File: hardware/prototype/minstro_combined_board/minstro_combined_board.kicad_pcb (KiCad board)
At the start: 4 copper layers, 130 x 100 mm, 130 parts, among them J1001 VFO, J301 BATT, J401 BOOT, J402 UART, J403 USB_C_Receptacle_USB2.0_16P, J404 SDMMC 4b, J405 Conn_Coaxial, J501 Headset, J601 FT6236_Conn_01x06, J602 ILI9488_Conn, J603 ST7789_Conn_01x12, J701 SOICbite-SWD, J801 NAV CONN, Q601 2N7002, SW401 RST, SW801 Navigation_Encoder_Joystick_S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, U201 LMR36006, U301 BQ24074RGT, U401 ESP32-S3, U402 W25Q128JVS, U701 ATSAMD10D13A-M, Y401 40 MHz

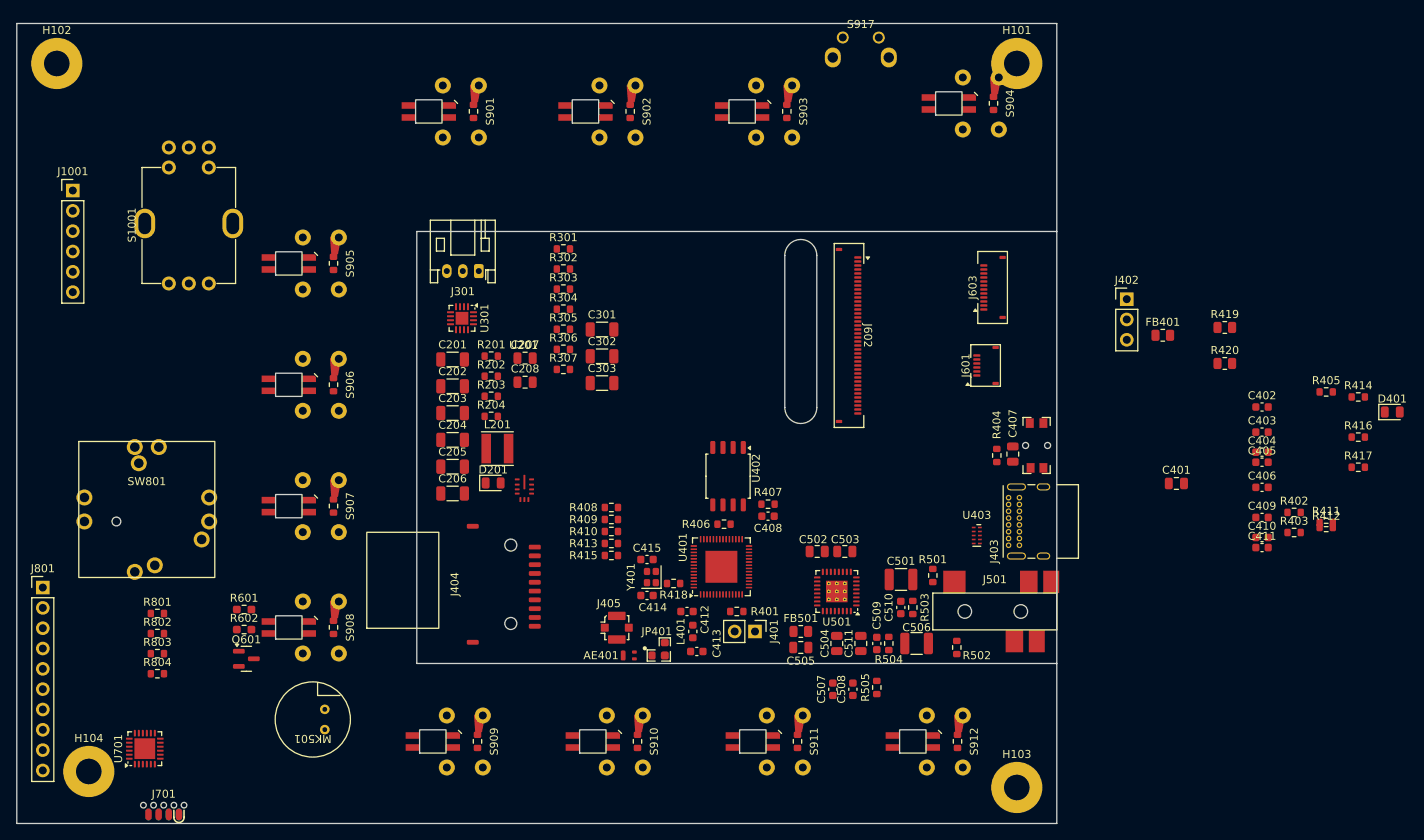
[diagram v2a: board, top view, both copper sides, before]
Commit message: Layout and routing Power and initial signals, SD card
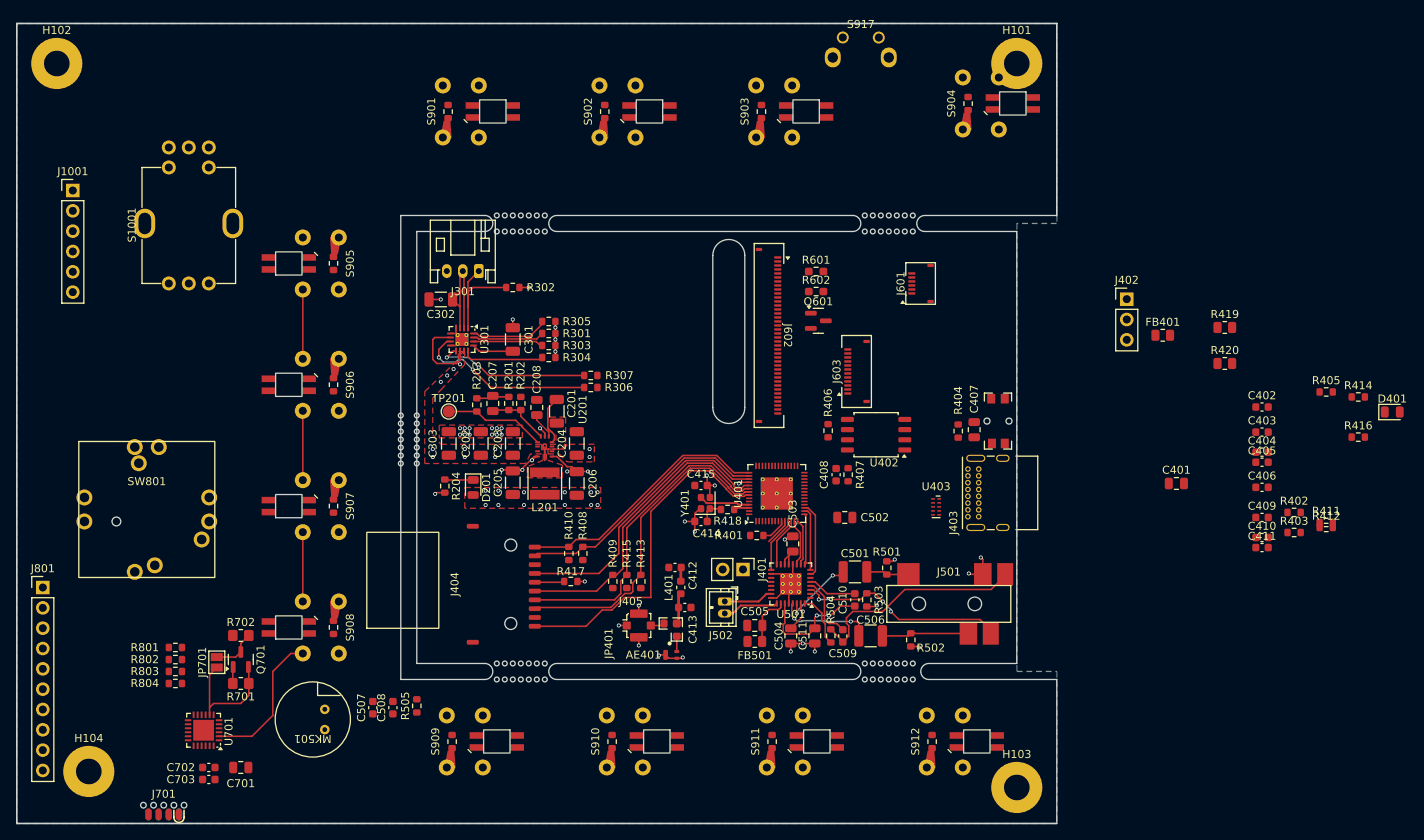
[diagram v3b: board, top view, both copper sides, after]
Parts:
- added C701: 10uF, Capacitor_SMD:C_0805_2012Metric, F.Cu at (93.0, 133.0)
- added C702: 0.1uF, Capacitor_SMD:C_0603_1608Metric, F.Cu at (89.0, 133.0)
- added C703: 0.1uF, Capacitor_SMD:C_0603_1608Metric, F.Cu at (89.0, 134.5)
- added J502: SPKR, Connector_JST:JST_ZH_B2B-ZR_1x02_P1.50mm_Vertical, F.Cu at (153.5, 112.2)
- added JP701: Jumper_2_Open, Jumper:SolderJumper-2_P1.3mm_Open_Pad1.0x1.5mm, F.Cu at (90.0, 119.8)
- added Q701: 2N7002, Package_TO_SOT_SMD:SOT-23, F.Cu at (93.0, 119.5)
- added R701: 10k, Resistor_SMD:R_0805_2012Metric_Pad1.20x1.40mm_HandSolder, F.Cu at (93.0, 122.5)
- added R702: 10k, Resistor_SMD:R_0805_2012Metric_Pad1.20x1.40mm_HandSolder, F.Cu at (93.0, 116.5)
- added REF**: Untitled, BVH_Features:MouseBite_2mm_7holes, F.Cu at (174.0, 65.0)
- added REF**: Untitled, BVH_Features:MouseBite_2mm_7holes, F.Cu at (174.0, 121.0)
- added REF**: Untitled, BVH_Features:MouseBite_2mm_7holes, F.Cu at (128.0, 65.0)
- added REF**: Untitled, BVH_Features:MouseBite_2mm_7holes, F.Cu at (128.0, 121.0)
- added REF**: Untitled, BVH_Features:MouseBite_2mm_7holes, F.Cu at (114.0, 92.0)
- added TP201: TestPoint, TestPoint:TestPoint_Pad_D1.5mm, F.Cu at (119.0, 88.5)
- U301: footprint Package_DFN_QFN:VQFN-16-1EP_3x3mm_P0.5mm_EP1.6x1.6mm -> Package_DFN_QFN:VQFN-16-1EP_3x3mm_P0.5mm_EP1.6x1.6mm_ThermalVias
- U401: footprint Package_DFN_QFN:QFN-56-1EP_7x7mm_P0.4mm_EP4x4mm -> Package_DFN_QFN:QFN-56-1EP_7x7mm_P0.4mm_EP4x4mm_ThermalVias
- moved R417 99.5 mm to (134.2, 109.8), turned to 180 degrees
- moved Q601 83.1 mm to (165.2, 77.2)
- moved R601 83.1 mm to (164.9, 71.0)
- moved R602 83.1 mm to (164.9, 73.5)
- moved C507 57.5 mm to (109.5, 125.5)
- moved R505 57.5 mm to (115.0, 125.3)
- moved C508 57.5 mm to (112.0, 125.5)
- moved C302 21.4 mm to (118.0, 74.5), turned to 180 degrees
- moved C303 20.6 mm to (119.0, 92.5), turned to 90 degrees
- moved J603 20.0 mm to (170.0, 83.5)
- moved U402 19.2 mm to (172.4, 91.4), turned to 180 degrees
- moved R406 17.5 mm to (166.4, 90.9), turned to -90 degrees
- moved C206 15.6 mm to (135.0, 97.5), turned to 90 degrees
- moved C204 15.5 mm to (135.0, 92.5), turned to 90 degrees
- moved C201 14.5 mm to (132.5, 88.5), turned to -90 degrees
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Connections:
- C511 pad 2: GNDA -> GND
- J301 pad 1: GND -> /Battery/BATT_TS
- J301 pad 3: /Battery/BATT_TS -> GND
- U401 pad 13: /Display Connectors/DISP_DC -> /Audio/I2S_MCLK
- U401 pad 14: /Display Connectors/DISP_CS -> /Audio/I2S_ADCIN
- U401 pad 15: /Display Connectors/DISP_SCL -> /Audio/I2S_ADCOUT
- U401 pad 16: /Display Connectors/DISP_SDA -> /Audio/I2S_BCLK
- U401 pad 17: /Display Connectors/DISP_RST -> /Audio/I2S_FS
- U401 pad 18: /Display Connectors/DISP_TS_INT -> /Display Connectors/DISP_DC
- U401 pad 19: /Display Connectors/DISP_TS_RST -> /Display Connectors/DISP_SCL
- U401 pad 21: /Battery/PWR_CHRG -> /Display Connectors/DISP_TS_INT
- U401 pad 22: /Battery/PWR_GOOD -> /Display Connectors/DISP_TS_RST
- U401 pad 23: unconnected-(U401-GPIO17-Pad23) -> /Display Connectors/DISP_SDA
- U401 pad 24: /ESP32 Microcontroller/SD_DET -> /Display Connectors/DISP_RST
- U401 pad 27: /Display Connectors/DISP_BL -> /Display Connectors/DISP_CS
- U401 pad 38: /Audio/I2S_FS -> /Display Connectors/DISP_BL
- U401 pad 39: /Audio/I2S_BCLK -> unconnected-(U401-GPIO34-Pad39)
- U401 pad 40: /Audio/I2S_ADCOUT -> unconnected-(U401-GPIO35-Pad40)
- U401 pad 41: /Audio/I2S_ADCIN -> /Battery/PWR_CHRG
- U401 pad 42: /Audio/I2S_MCLK -> /Battery/PWR_GOOD
- U401 pad 43: /ESP32 Microcontroller/SD_SCK -> /ESP32 Microcontroller/SD_DAT1
- U401 pad 45: /ESP32 Microcontroller/SD_DAT1 -> /ESP32 Microcontroller/SD_SCK
- U401 pad 47: /ESP32 Microcontroller/SD_DAT2 -> /ESP32 Microcontroller/SD_CMD
- U401 pad 49: /ESP32 Microcontroller/UART_TX -> /ESP32 Microcontroller/SD_DAT2
- U401 pad 50: /ESP32 Microcontroller/UART_RX -> /ESP32 Microcontroller/SD_DET
- U401 pad 51: /ESP32 Microcontroller/SD_CMD -> unconnected-(U401-GPIO45-Pad51)
- U401 pad 52: /ESP32 Microcontroller/SD_DET -> unconnected-(U401-GPIO46-Pad52)
- U501 pad 24: GNDA -> GND
- U501 pad 33: (no net) -> GND
- U701 pad 1: /HMI Controller/ROW_A -> /HMI Controller/ROW_C
- U701 pad 3: /HMI Controller/ROW_C -> unconnected-(U701-PA04-Pad3)
- U701 pad 4: /HMI Controller/ROW_D -> /HMI Controller/ROW_A
- U701 pad 8: /HMI Controller/RGB_DATA -> /HMI Controller/RGB_DATA_3.3
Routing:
- net GND: track 0.00 -> 59.3 mm, vias 0 -> 42
- net /HMI Controller/ROW_B: track 0.00 -> 44.0 mm
- net /ESP32 Microcontroller/SD_DET: track 0.00 -> 42.6 mm
- net /ESP32 Microcontroller/SD_DAT2: track 0.00 -> 40.4 mm
- net /ESP32 Microcontroller/SD_DAT3: track 0.00 -> 39.6 mm
- net /ESP32 Microcontroller/SD_CMD: track 0.00 -> 38.0 mm
- net /ESP32 Microcontroller/SD_SCK: track 0.00 -> 35.5 mm
- net /ESP32 Microcontroller/SD_DAT0: track 0.00 -> 32.8 mm
- net /ESP32 Microcontroller/SD_DAT1: track 0.00 -> 32.4 mm
- net /Audio/Mic_HS: track 0.00 -> 27.9 mm
- net /Audio/R_HS_N: track 0.00 -> 26.2 mm, vias 0 -> 4
- net /Battery/PWR_GOOD: track 0.00 -> 22.9 mm, vias 0 -> 2
- net /Battery/PWR_CHRG: track 0.00 -> 19.6 mm, vias 0 -> 2
- net +3.3V: track 0.00 -> 17.5 mm, vias 0 -> 16
- net +BATT: track 0.00 -> 17.1 mm
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- added copper zone on F.Cu, net +3.3V
- added copper zone on In2.Cu, net +3.3V
- added copper zone on F.Cu, net /Power/SW
- added copper zone on B.Cu, net GND
- added copper zone on F.Cu, net GND
- added copper zone on In1.Cu, net GND
- added copper zone on F.Cu, net Vdrive
- added copper zone on In2.Cu, net Vdrive
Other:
- outline, holes or cut-outs redrawn

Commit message: Layout WIP
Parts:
- moved C402 25.8 mm to (212.7, 112.5)
- moved C403 25.8 mm to (212.7, 115.6)
- moved C404 25.8 mm to (212.7, 118.1)
- moved C405 25.8 mm to (212.7, 119.4)
- moved C406 25.8 mm to (212.7, 122.5)
- moved R414 4.32 mm to (237.0, 86.5)
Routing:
- net /ESP32 Microcontroller/CHIP_EN: track 0.00 -> 11.7 mm
- net GND: track 59.3 -> 63.6 mm, vias 42 -> 45
- net +3.3V: track 17.5 -> 18.7 mm, vias 16 -> 17
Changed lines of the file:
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@@
 	(footprint "Capacitor_SMD:C_0603_1608Metric"
 		(layer "F.Cu")
-		(at 220.655 97.98)
+		(at 212.725 122.5)
 		(descr "Capacitor SMD 0603 (1608 Metric), square (rectangular) end terminal, IPC-7351 nominal, (Body size source: IPC-SM-782 page 76, https://www.pcb-3d.com/wordpress/wp-content/uploads/ipc-sm-782a_amendment_1_and_2.pdf), generated with kicad-footprint-generator")
 		(tags "capacitor")
@@
 	(footprint "Capacitor_SMD:C_0603_1608Metric"
 		(layer "F.Cu")
-		(at 220.655 87.94)
+		(at 212.725 112.46)
 		(descr "Capacitor SMD 0603 (1608 Metric), square (rectangular) end terminal, IPC-7351 nominal, (Body size source: IPC-SM-782 page 76, https://www.pcb-3d.com/wordpress/wp-content/uploads/ipc-sm-782a_amendment_1_and_2.pdf), generated with kicad-footprint-generator")
 		(tags "capacitor")
@@
 	(footprint "Capacitor_SMD:C_0603_1608Metric"
 		(layer "F.Cu")
-		(at 220.655 93.5875)
+		(at 212.725 118.1075)
 		(descr "Capacitor SMD 0603 (1608 Metric), square (rectangular) end terminal, IPC-7351 nominal, (Body size source: IPC-SM-782 page 76, https://www.pcb-3d.com/wordpress/wp-content/uploads/ipc-sm-782a_amendment_1_and_2.pdf), generated with kicad-footprint-generator")
 		(tags "capacitor")
@@
 		(tags "LED")
 		(property "Reference" "D401"
-			(at 0 -1.65 0)
+			(at -3.435 -0.0675 0)
 			(layer "F.SilkS")
 			(effects
@@
 	(footprint "Capacitor_SMD:C_0603_1608Metric"
 		(layer "F.Cu")
-		(at 220.655 94.8425)
+		(at 212.725 119.3625)
 		(descr "Capacitor SMD 0603 (1608 Metric), square (rectangular) end terminal, IPC-7351 nominal, (Body size source: IPC-SM-782 page 76, https://www.pcb-3d.com/wordpress/wp-content/uploads/ipc-sm-782a_amendment_1_and_2.pdf), generated with kicad-footprint-generator")
 		(tags "capacitor")
@@
 	(footprint "Resistor_SMD:R_0603_1608Metric"
 		(layer "F.Cu")
-		(at 232.685 86.685)
+		(at 237 86.5)
 		(descr "Resistor SMD 0603 (1608 Metric), square (rectangular) end terminal, IPC-7351 nominal, (Body size source: IPC-SM-782 page 72, https://www.pcb-3d.com/wordpress/wp-content/uploads/ipc-sm-782a_amendment_1_and_2.pdf), generated with kicad-footprint-generator")
 		(tags "resistor")
 		(property "Reference" "R414"
-			(at 0 -1.43 0)
+			(at -3.5 0 0)
 			(layer "F.SilkS")
 			(effects
@@
 	(footprint "Capacitor_SMD:C_0603_1608Metric"
 		(layer "F.Cu")
-		(at 220.655 91.0775)
+		(at 212.725 115.5975)
 		(descr "Capacitor SMD 0603 (1608 Metric), square (rectangular) end terminal, IPC-7351 nominal, (Body size source: IPC-SM-782 page 76, https://www.pcb-3d.com/wordpress/wp-content/uploads/ipc-sm-782a_amendment_1_and_2.pdf), generated with kicad-footprint-generator")
 		(tags "capacitor")
@@
 	)
 	(segment
+		(start 186 92.5)
+		(end 185.5 93)
+		(width 0.2)
+		(layer "F.Cu")
+		(net 1)
+	)
+	(segment
 		(start 185.75 108.85)
 		(end 185.75 107)
@@
 	)
 	(segment
+		(start 184.675 88.825)
+		(end 185 88.5)
+		(width 0.2)
+		(layer "F.Cu")
+		(net 1)
+	)
+	(segment
 		(start 161.5 111.3)
 		(end 161.75 111.05)
@@
 	)
 	(segment
+		(start 186.8 86.9)
+		(end 186.8 87.7)
+		(width 0.2)
+		(layer "F.Cu")
+		(net 1)
+	)
+	(segment
 		(start 161.75 117.5)
 		(end 163.25 117.5)
@@
 	)
 	(segment
+		(start 184.675 89.825)
+		(end 184.675 88.825)
+		(width 0.2)
+		(layer "F.Cu")
+		(net 1)
+	)
+	(segment
 		(start 161.4 104.1)
 		(end 161 104.5)
@@
 	)
 	(segment
+		(start 186.9 92.5)
+		(end 186 92.5)
+		(width 0.2)
+		(layer "F.Cu")
+		(net 1)
+	)
+	(segment
 		(start 164.75 117.5)
 		(end 164.75 118.5)
@@
 	)
 	(segment
+		(start 186.8 87.7)
+		(end 186.5 88)
+		(width 0.2)
+		(layer "F.Cu")
+		(net 1)
+	)
+	(segment
 		(start 149.75 102.25)
 		(end 149.75 101.25)
@@
 	)
 	(via
+		(at 185 88.5)
+		(size 0.5)
+		(drill 0.3)
+		(layers "F.Cu" "B.Cu")
+		(net 1)
+	)
+	(via
 		(at 177.75 118)
 		(size 0.5)
@@
 	)
 	(via
+		(at 185.5 93)
+		(size 0.5)
+		(drill 0.3)
+		(layers "F.Cu" "B.Cu")
+		(net 1)
+	)
+	(via
 		(at 142.75 112.75)
 		(size 0.5)
@@
 	)
 	(via
+		(at 186.5 88)
+		(size 0.5)
+		(drill 0.3)
+		(layers "F.Cu" "B.Cu")
+		(net 1)
+	)
+	(via
 		(at 161 104.5)
 		(size 0.5)
@@
 	)
 	(segment
+		(start 182.675 90.125)
+		(end 182.675 89.175)
+		(width 0.2)
+		(layer "F.Cu")
+		(net 6)
+	)
+	(segment
 		(start 163.25 114.1)
 		(end 163.25 113.5)
@@
 	)
 	(segment
+		(start 182.675 89.175)
+		(end 182.5 89)
+		(width 0.2)
+		(layer "F.Cu")
+		(net 6)
+	)
+	(segment
 		(start 124.55 86.55)
 		(end 124.675 86.675)
@@
 	)
 	(via
+		(at 182.5 89)
+		(size 0.5)
+		(drill 0.3)
+		(layers "F.Cu" "B.Cu")
+		(net 6)
+	)
+	(via
 		(at 136 109.75)
 		(size 0.5)
@@
 	)
 	(segment
+		(start 188.249 87.151)
+		(end 188.5 86.9)
+		(width 0.2)
+		(layer "F.Cu")
+		(net 12)
+	)
+	(segment
+		(start 182.725 91.725)
+		(end 182.675 91.775)
+		(width 0.2)
+		(layer "F.Cu")
+		(net 12)
+	)
+	(segment
+		(start 184.675 91.725)
+		(end 185.4 91)
+		(width 0.2)
+		(layer "F.Cu")
+		(net 12)
+	)
+	(segment
+		(start 188.249 91)
+		(end 188.249 87.151)
+		(width 0.2)
+		(layer "F.Cu")
+		(net 12)
+	)
+	(segment
+		(start 185.4 91)
+		(end 188.249 91)
+		(width 0.2)
+		(layer "F.Cu")
+		(net 12)
+	)
+	(segment
+		(start 188.249 92.249)
+		(end 188.249 91)
+		(width 0.2)
+		(layer "F.Cu")
+		(net 12)
+	)
+	(segment
+		(start 188.5 92.5)
+		(end 188.249 92.249)
+		(width 0.2)
+		(layer "F.Cu")
+		(net 12)
+	)
+	(segment
+		(start 184.675 91.725)
+		(end 182.725 91.725)
+		(width 0.2)
+		(layer "F.Cu")
+		(net 12)
+	)
+	(segment

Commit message: Routing mostly completed
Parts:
- removed J402: UART, Connector_PinHeader_2.54mm:PinHeader_1x03_P2.54mm_Vertical
- removed R403: 100k, Resistor_SMD:R_0603_1608Metric
- removed R405: 499, Resistor_SMD:R_0603_1608Metric
- J1001: footprint Connector_PinHeader_2.54mm:PinHeader_1x06_P2.54mm_Vertical -> BVH_PinHeader_FrictionRetention:PinHeader_1x06_P2.54mm_Vertical
- J403: footprint Connector_USB:USB_C_Receptacle_GCT_USB4085 -> BVH_Connectors_Misc:USB_C_Receptacle_GCT_USB4085_PinPaste
- J601: value FT6236_Conn_01x06 -> FT6236
- J602: value ILI9488_Conn -> ILI9488
- J603: value ST7789_Conn_01x12 -> ST7789
- J801: footprint Connector_PinHeader_2.54mm:PinHeader_1x10_P2.54mm_Vertical -> BVH_PinHeader_FrictionRetention:PinHeader_1x10_P2.54mm_Vertical
- REF** (x3): footprint BVH_Features:MouseBite_2mm_7holes -> BVH_Features:MouseBite_2mm_4holes_Wide
- moved D401 87.0 mm to (152.1, 107.8)
- moved C411 86.6 mm to (134.2, 111.2)
- moved R419 75.0 mm to (142.0, 90.1), turned to 90 degrees
- moved R420 72.4 mm to (144.0, 90.1), turned to 90 degrees
- moved C401 70.4 mm to (140.0, 90.0), turned to 90 degrees
- moved R402 69.7 mm to (155.3, 108.0)
- moved FB401 66.4 mm to (147.2, 105.1)
- moved C507 64.8 mm to (174.3, 127.1), turned to 180 degrees
- moved C508 62.3 mm to (174.3, 125.5), turned to 180 degrees
- moved C406 62.0 mm to (153.6, 103.8), turned to 180 degrees
- moved C403 61.6 mm to (154.6, 95.2), turned to 90 degrees
- moved C405 61.5 mm to (153.6, 102.3), turned to 180 degrees
- moved R505 56.9 mm to (171.9, 126.2), turned to -90 degrees
- moved C402 56.0 mm to (157.3, 104.5)
- moved R414 55.7 mm to (184.8, 105.8)
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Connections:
- C202 pad 1: Vdrive -> +5V
- C203 pad 1: Vdrive -> +5V
- C204 pad 1: Vdrive -> +5V
- C303 pad 1: Vdrive -> +5V
- FB501 pad 1: Vdrive -> +5V
- H101 pad 1: (no net) -> GND
- H102 pad 1: (no net) -> GND
- H103 pad 1: (no net) -> GND
- H104 pad 1: (no net) -> GND
- J601 pad MP: (no net) -> unconnected-(J601-PadMP)
- J602 pad MP: (no net) -> unconnected-(J602-PadMP)
- J603 pad MP: (no net) -> unconnected-(J603-PadMP)
- U201 pad 10: Vdrive -> +5V
- U201 pad 2: Vdrive -> +5V
- U201 pad 9: Vdrive -> +5V
- U301 pad 10: Vdrive -> +5V
- U301 pad 11: Vdrive -> +5V
- U301 pad 6: Vdrive -> +5V
- U401 pad 39: unconnected-(U401-GPIO34-Pad39) -> /Battery/PWR_CHRG
- U401 pad 40: unconnected-(U401-GPIO35-Pad40) -> /Battery/PWR_GOOD
- U401 pad 41: /Battery/PWR_CHRG -> /ESP32 Microcontroller/HMI_WAKE
- U401 pad 42: /Battery/PWR_GOOD -> /ESP32 Microcontroller/HMI_INT
- U401 pad 6: /ESP32 Microcontroller/MODE_SEL -> unconnected-(U401-GPIO1-Pad6)
- U401 pad 7: /ESP32 Microcontroller/HMI_WAKE -> unconnected-(U401-GPIO2-Pad7)
- U401 pad 8: /ESP32 Microcontroller/HMI_INT -> unconnected-(U401-GPIO3-Pad8)
- U403 pad 1: unconnected-(U403-CH1-Pad1) -> /ESP32 Microcontroller/USB_N
- U403 pad 4: /ESP32 Microcontroller/USB_P -> unconnected-(U403-CH3-Pad4)
- U403 pad 5: /ESP32 Microcontroller/USB_N -> /ESP32 Microcontroller/USB_P
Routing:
- net +3.3V: track 18.7 -> 145.9 mm, vias 17 -> 41
- net /I2C_SDA: track 6.97 -> 118.8 mm, vias 0 -> 3
- net /I2C_SCL: track 6.15 -> 115.8 mm, vias 0 -> 3
- net /HMI Controller/ROW_C: track 0.00 -> 104.3 mm, vias 0 -> 2
- net Net-(S904B-DO): track 0.00 -> 102.3 mm
- net +5V: track 0.00 -> 97.7 mm, vias 0 -> 25
- net /Battery/Vusb: track 5.21 -> 102.1 mm, vias 0 -> 1
- net /Audio/Mic_HS_N: track 14.9 -> 98.6 mm
- net GND: track 63.6 -> 137.9 mm, vias 45 -> 104
- net /Audio/Mic_P: track 0.00 -> 67.6 mm
- net /ESP32 Microcontroller/HMI_WAKE: track 0.00 -> 51.2 mm
- net /ESP32 Microcontroller/HMI_INT: track 0.00 -> 50.7 mm
- net Net-(S908B-DO): track 0.00 -> 48.0 mm, vias 0 -> 2
- net /Display Connectors/DISP_CS: track 0.00 -> 41.5 mm, vias 0 -> 4
- net /Display Connectors/DISP_DC: track 0.00 -> 40.8 mm, vias 0 -> 3
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- added copper zone on F.Cu, net +5V
- added copper zone on In2.Cu, net +5V
- removed copper zone on F.Cu, net Vdrive
- removed copper zone on In2.Cu, net Vdrive
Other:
- outline, holes or cut-outs redrawn
